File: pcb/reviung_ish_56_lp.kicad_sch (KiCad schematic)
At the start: 128 parts, among them SW02 SW_Push, U1 ProMicro

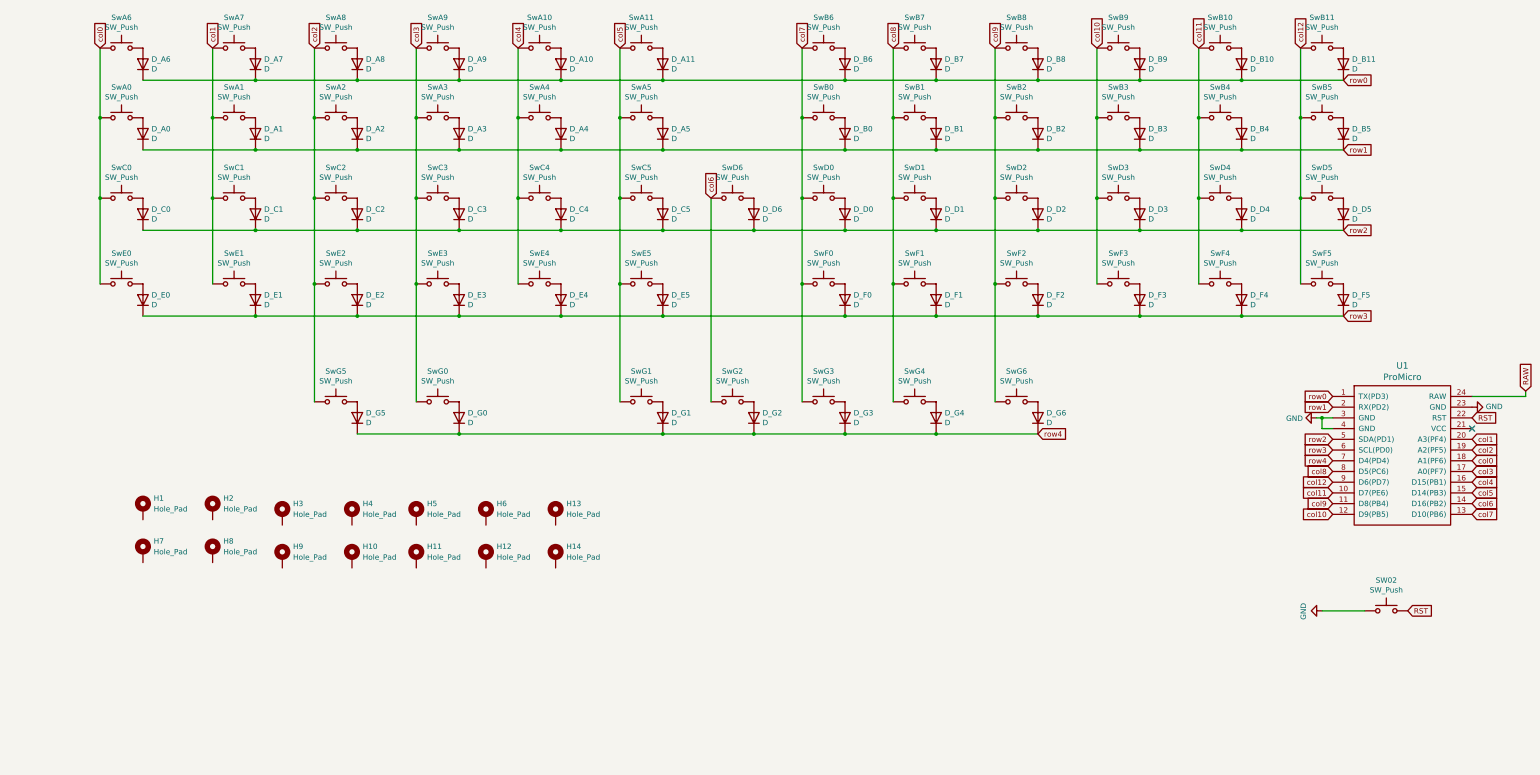
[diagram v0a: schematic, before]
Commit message: Make outline more like Reviung41; chage bottom row mods to 1u; neater col/row routing
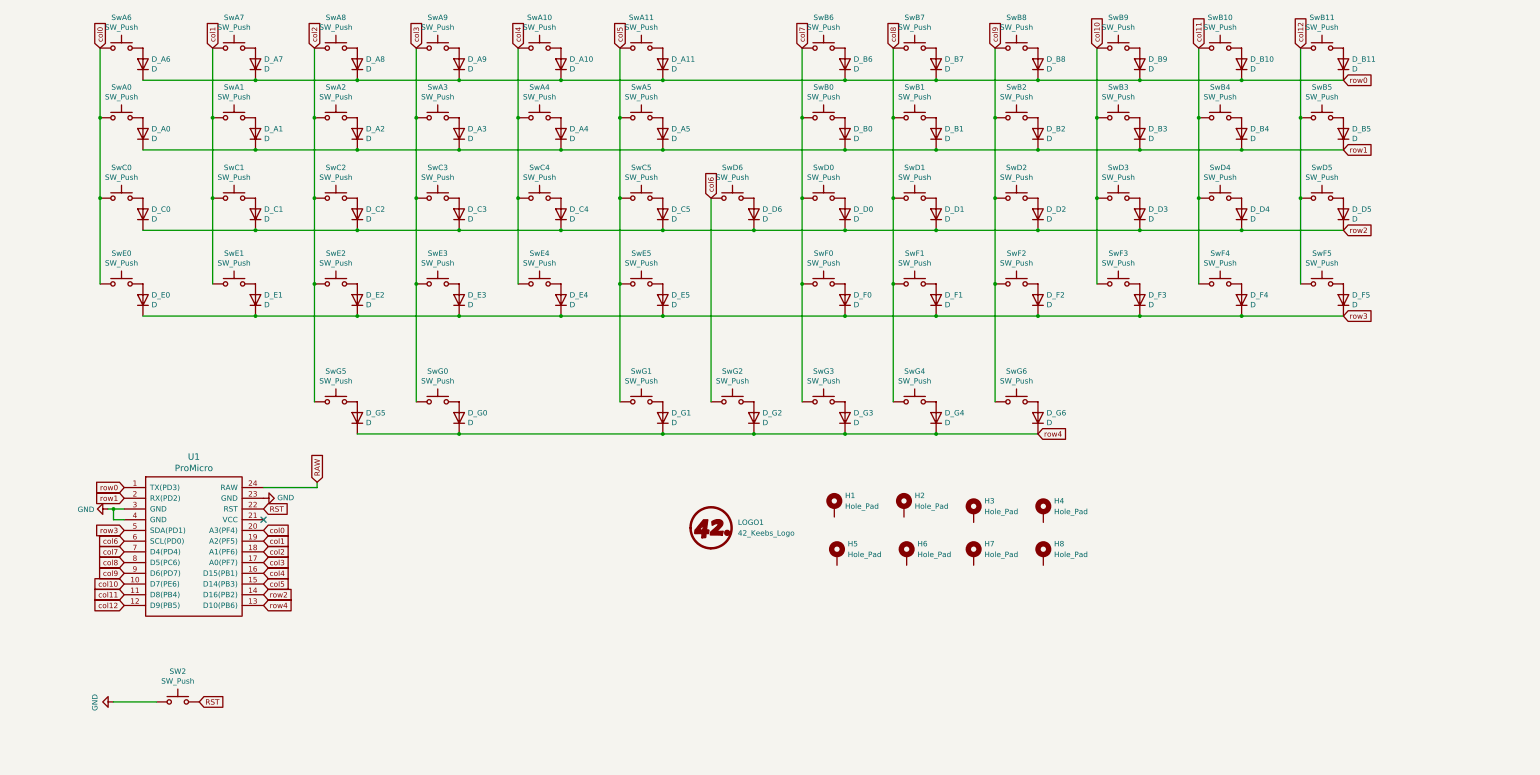
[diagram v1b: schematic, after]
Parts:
- removed H10, H11, H12, H13, H14, H9: Hole_Pad, General_footprints:Mount_M2, symbol horizon-components:Hole_Pad
- added LOGO1: 42_Keebs_Logo, 42keebs:42Keebs-icon-10mm-Mask, symbol 42keebs:42_Keebs_Logo
- renumbered SW02 to SW2
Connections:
- net col0: now also U1.20 (A3(PF4)); no longer U1.18 (A1(PF6))
- net col1: now also U1.19 (A2(PF5)); no longer U1.20 (A3(PF4))
- net col10: now also U1.10 (D7(PE6)); no longer U1.12 (D9(PB5))
- net col11: now also U1.11 (D8(PB4)); no longer U1.10 (D7(PE6))
- net col12: now also U1.12 (D9(PB5)); no longer U1.9 (D6(PD7))
- net col2: now also U1.18 (A1(PF6)); no longer U1.19 (A2(PF5))
- net col6: now also U1.6 (SCL(PD0)); no longer U1.14 (D16(PB2))
- net col7: now also U1.7 (D4(PD4)); no longer U1.13 (D10(PB6))
- net col9: now also U1.9 (D6(PD7)); no longer U1.11 (D8(PB4))
- net row2: now also U1.14 (D16(PB2)); no longer U1.5 (SDA(PD1))
- net row3: now also U1.5 (SDA(PD1)); no longer U1.6 (SCL(PD0))
- net row4: now also U1.13 (D10(PB6)); no longer U1.7 (D4(PD4))
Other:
- moved on the sheet: H1, H2, H3, H4, H5, H6, H7, H8, SW2, U1

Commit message: Make diode footprints dual-sided
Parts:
- D_A0, D_A1, D_A10, D_A11, D_A2, D_A3, D_A4, D_A5, D_A6, D_A7, D_A8, D_A9, D_B0, D_B1, D_B10, D_B11, D_B2, D_B3, D_B4, D_B5, D_B6, D_B7, D_B8, D_B9, D_C0, D_C1, D_C2, D_C3, D_C4, D_C5, D_D0, D_D1, D_D2, D_D3, D_D4, D_D5, D_D6, D_E0, D_E1, D_E2, D_E3, D_E4, D_E5, D_F0, D_F1, D_F2, D_F3, D_F4, D_F5, D_G0, D_G1, D_G2, D_G3, D_G4, D_G5, D_G6: footprint General_footprints:Diode_SOD123 -> General_footprints:Diode_SOD123_dual_sided

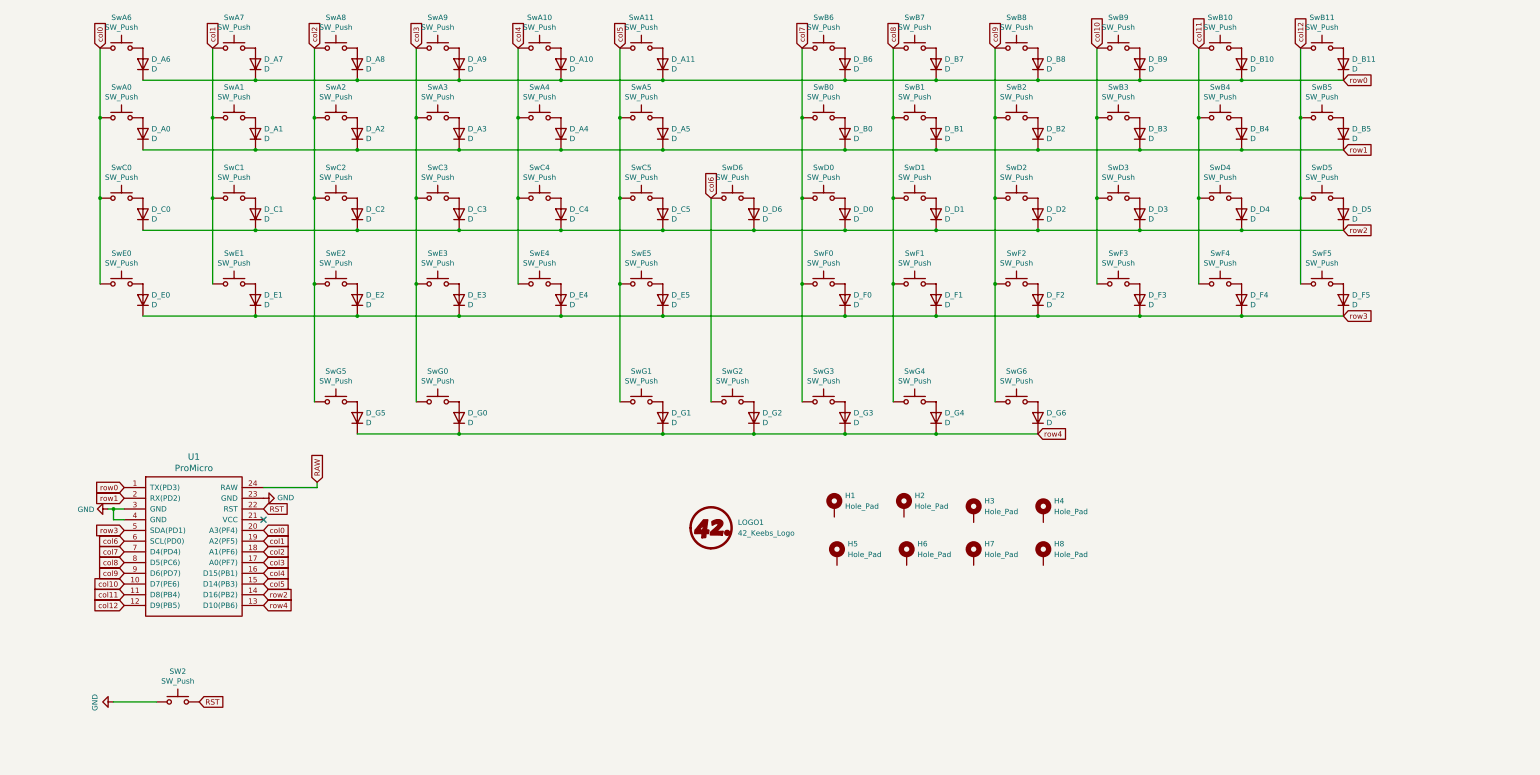
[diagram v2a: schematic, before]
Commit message: Move one bottom-row switch one column left in preparation for 2x1u space
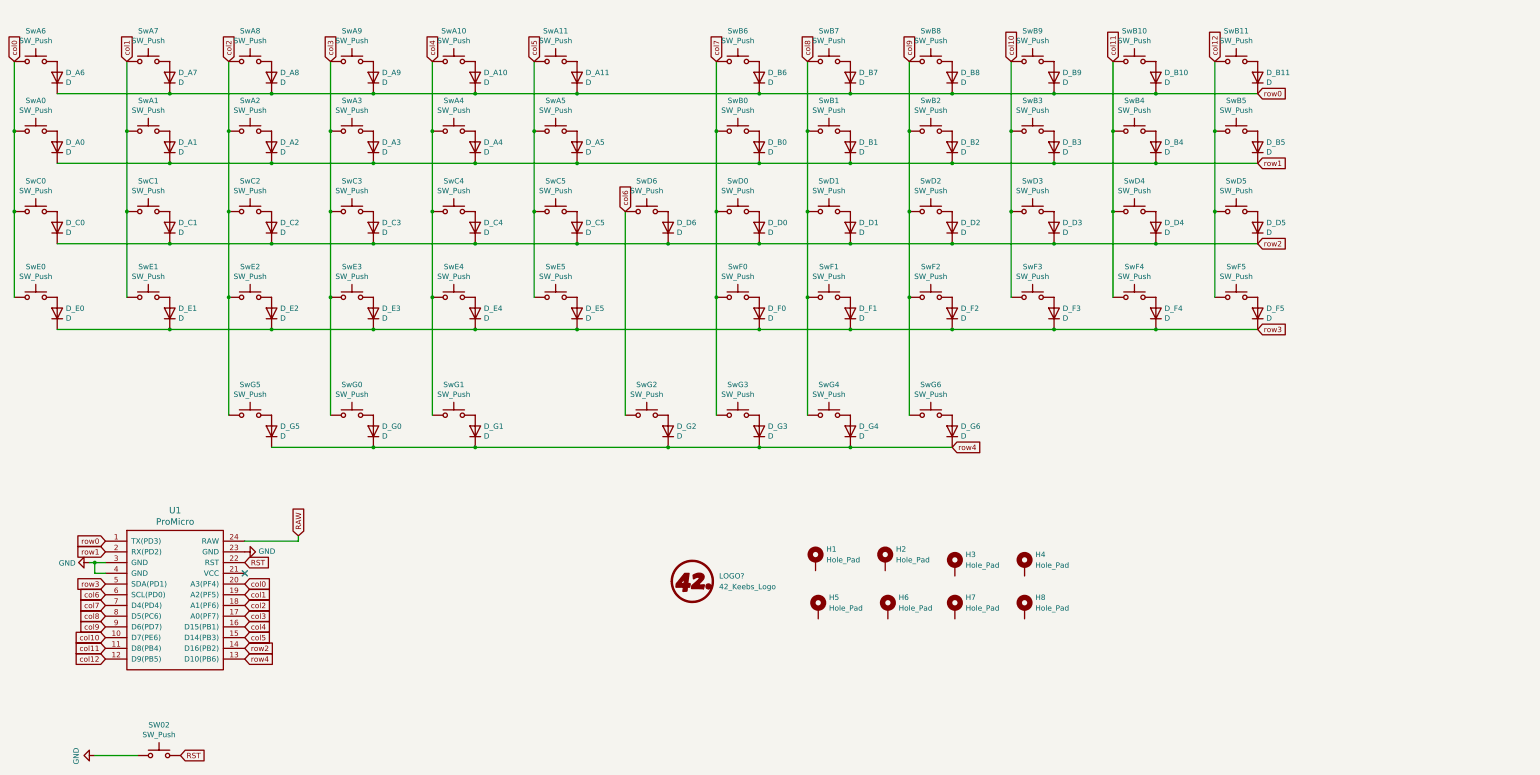
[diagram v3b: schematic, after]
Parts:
- D_A0, D_A1, D_A10, D_A11, D_A2, D_A3, D_A4, D_A5, D_A6, D_A7, D_A8, D_A9, D_B0, D_B1, D_B10, D_B11, D_B2, D_B3, D_B4, D_B5, D_B6, D_B7, D_B8, D_B9, D_C0, D_C1, D_C2, D_C3, D_C4, D_C5, D_D0, D_D1, D_D2, D_D3, D_D4, D_D5, D_D6, D_E0, D_E1, D_E2, D_E3, D_E4, D_E5, D_F0, D_F1, D_F2, D_F3, D_F4, D_F5, D_G0, D_G1, D_G2, D_G3, D_G4, D_G5, D_G6: footprint General_footprints:Diode_SOD123_dual_sided -> General_footprints:Diode_SOD123
- renumbered LOGO1 to LOGO?, SW2 to SW02
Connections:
- net col4: now also SwG1.1
- net col5: no longer SwG1.1
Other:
- moved on the sheet: D_A0, D_A1, D_A10, D_A11, D_A2, D_A3, D_A4, D_A5, D_A6, D_A7, D_A8, D_A9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

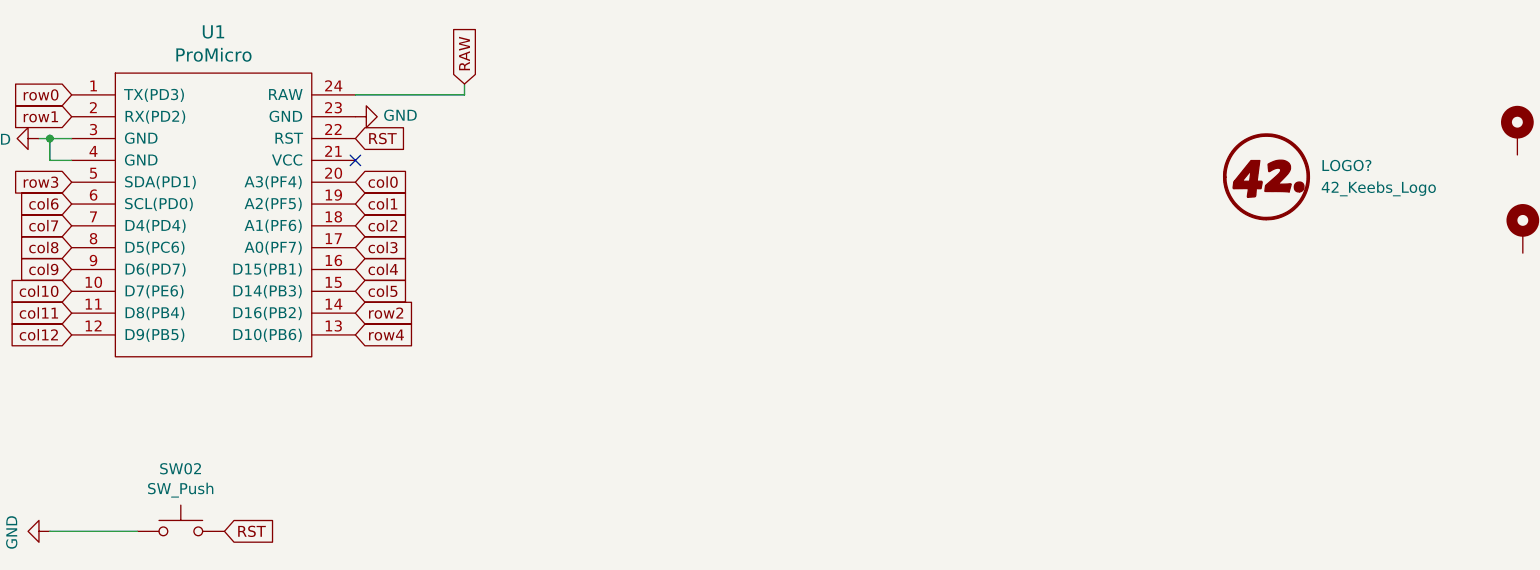
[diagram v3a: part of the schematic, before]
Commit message: Make diode footprints dual-sided again
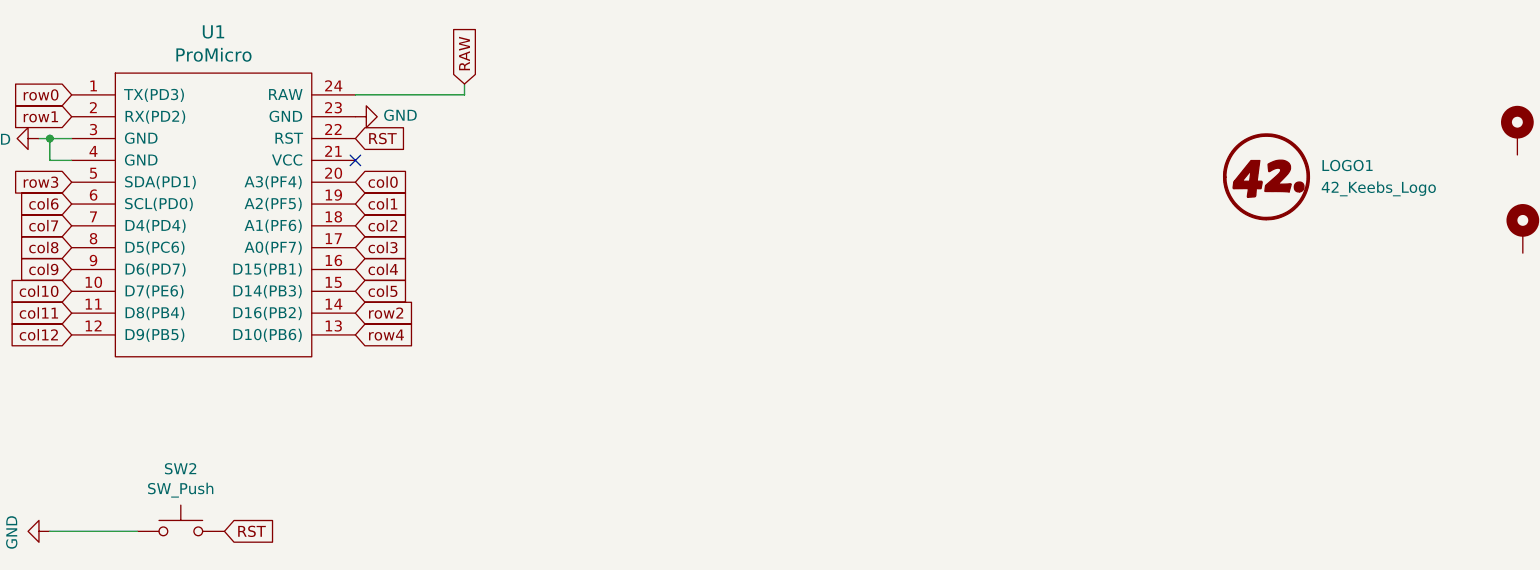
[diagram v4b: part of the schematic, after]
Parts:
- D_A0, D_A1, D_A10, D_A11, D_A2, D_A3, D_A4, D_A5, D_A6, D_A7, D_A8, D_A9, D_B0, D_B1, D_B10, D_B11, D_B2, D_B3, D_B4, D_B5, D_B6, D_B7, D_B8, D_B9, D_C0, D_C1, D_C2, D_C3, D_C4, D_C5, D_D0, D_D1, D_D2, D_D3, D_D4, D_D5, D_D6, D_E0, D_E1, D_E2, D_E3, D_E4, D_E5, D_F0, D_F1, D_F2, D_F3, D_F4, D_F5, D_G0, D_G1, D_G2, D_G3, D_G4, D_G5, D_G6: footprint General_footprints:Diode_SOD123 -> General_footprints:Diode_SOD123_dual_sided
- gave numbers to parts that had none: 1
- renumbered SW02 to SW2

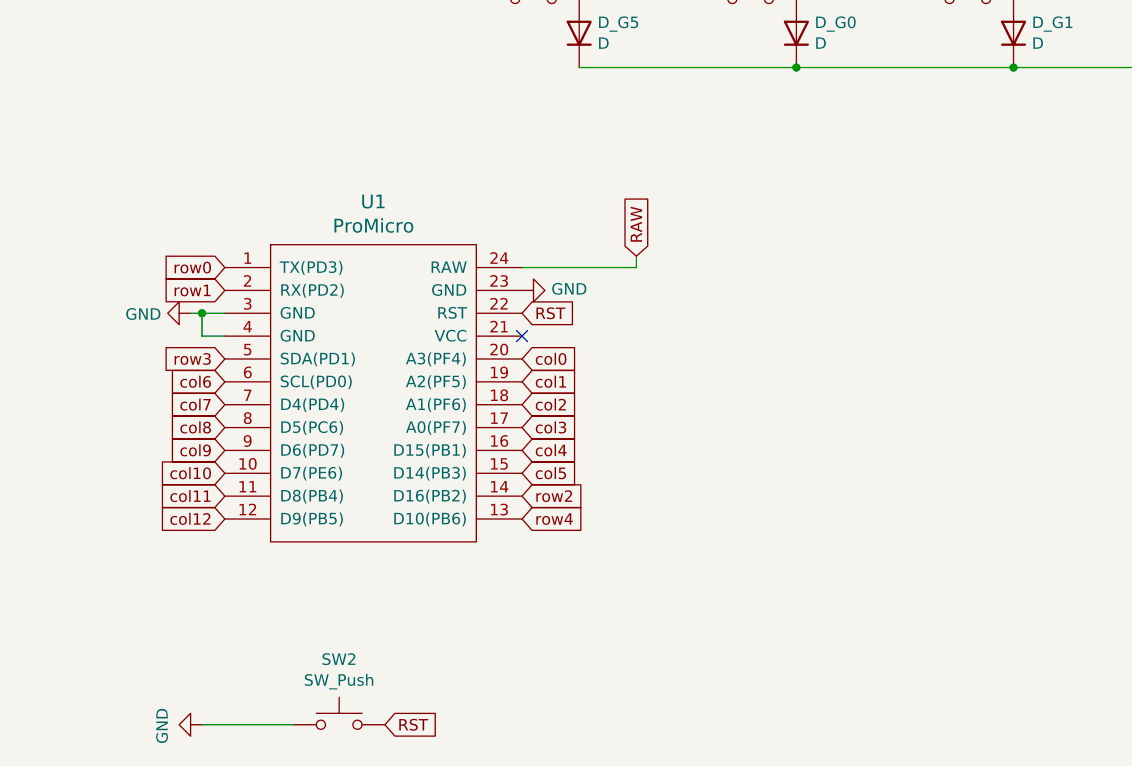
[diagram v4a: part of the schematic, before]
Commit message: Add power switch and battery connectors; update Pro Micro and some switch footprints
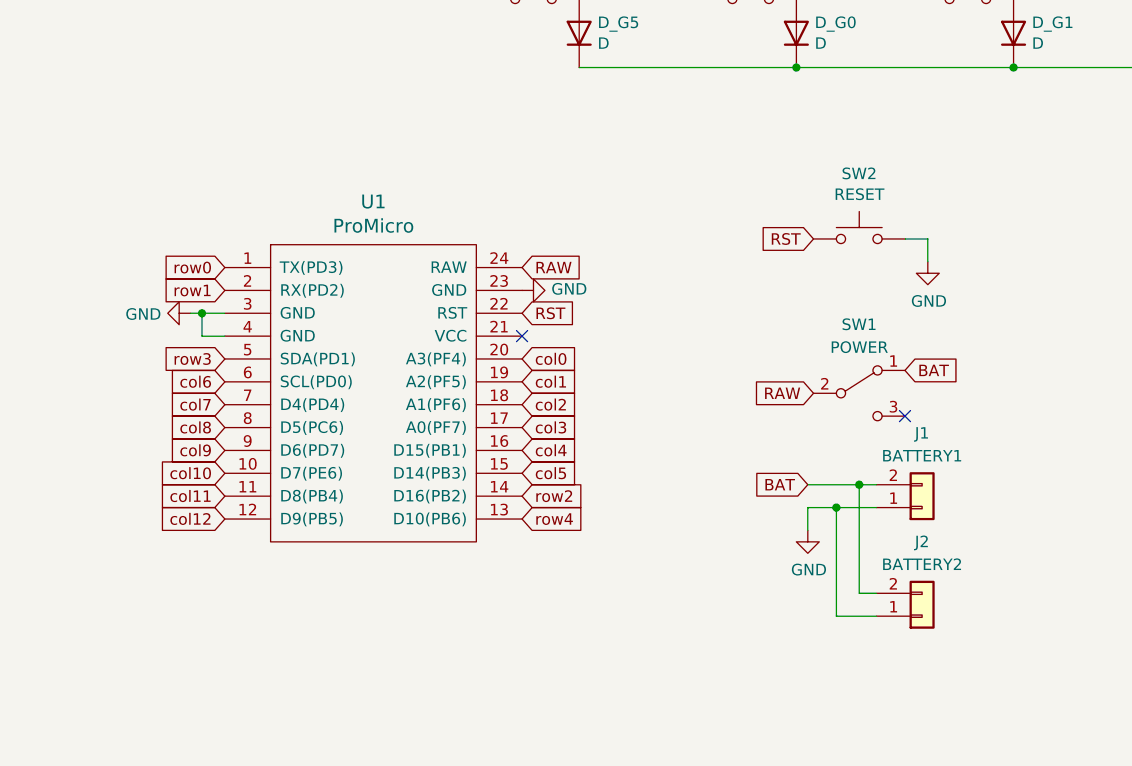
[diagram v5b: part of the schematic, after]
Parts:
- added J1: BATTERY1, Connector_PinHeader_2.54mm:PinHeader_1x02_P2.54mm_Vertical, symbol Connector_Generic:Conn_01x02
- added J2: BATTERY2, Connector_JST:JST_PH_S2B-PH-K_1x02_P2.00mm_Horizontal, symbol Connector_Generic:Conn_01x02
- added SW1: POWER, Button_Switch_THT:SW_CuK_JS202011AQN_DPDT_Angled, symbol Switch:SW_SPDT
- SW2: value SW_Push -> RESET; footprint General_footprints:TACT_SWITCH_ONE_SIDE -> Button_Switch_SMD:SW_SPST_TL3342
- SwA0, SwA1, SwA10, SwA11, SwA2, SwA3, SwA4, SwA5, SwA6, SwA7, SwA8, SwA9, SwB0, SwB1, SwB10, SwB11, SwB2, SwB3, SwB4, SwB5, SwB6, SwB7, SwB8, SwB9, SwC0, SwC1, SwC2, SwC3, SwC4, SwC5, SwD0, SwD1, SwD2, SwD3, SwD4, SwD5, SwD6, SwE0, SwE1, SwE2, SwE3, SwE4, SwE5, SwF0, SwF1, SwF2, SwF3, SwF4, SwF5, SwG0, SwG1, SwG3, SwG4, SwG5, SwG6: footprint General_footprints:Kailh_socket_PG1350 -> 42keebs:Kailh_socket_PG1350
- U1: footprint keeblib:ArduinoProMicro -> 42keebs:ProMicro-USB-C
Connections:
- net GND: now also SW2.2, J1.1 (Pin_1), J2.1 (Pin_1); no longer SW2.1
- net RAW: now also SW1.2 (B)
- net RST: now also SW2.1; no longer SW2.2
- new net BAT: J1.2 (Pin_2), J2.2 (Pin_2), SW1.1 (A)
- no-connect marks 1 -> 2
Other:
- moved on the sheet: SW2

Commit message: Use diode footprints from 42. Keebs lib; switch to standard hole footprints
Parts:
- D_A0, D_A1, D_A10, D_A11, D_A2, D_A3, D_A4, D_A5, D_A6, D_A7, D_A8, D_A9, D_B0, D_B1, D_B10, D_B11, D_B2, D_B3, D_B4, D_B5, D_B6, D_B7, D_B8, D_B9, D_C0, D_C1, D_C2, D_C3, D_C4, D_C5, D_D0, D_D1, D_D2, D_D3, D_D4, D_D5, D_D6, D_E0, D_E1, D_E2, D_E3, D_E4, D_E5, D_F0, D_F1, D_F2, D_F3, D_F4, D_F5, D_G0, D_G1, D_G2, D_G3, D_G4, D_G5, D_G6: footprint General_footprints:Diode_SOD123_dual_sided -> 42keebs:Diode_SOD123_dual_sided
- H1, H2, H3, H4, H5, H6, H7, H8: footprint General_footprints:Mount_M2 -> MountingHole:MountingHole_2.2mm_M2_Pad_Via
